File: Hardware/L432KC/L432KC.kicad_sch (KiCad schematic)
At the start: 26 parts, among them J1 Conn_01x09, J2 Conn_01x07, J3 USB_B_Micro, J4 JVCC, J5 JTAG, J6 LogicAna, U1 NUCLEO-L432KC

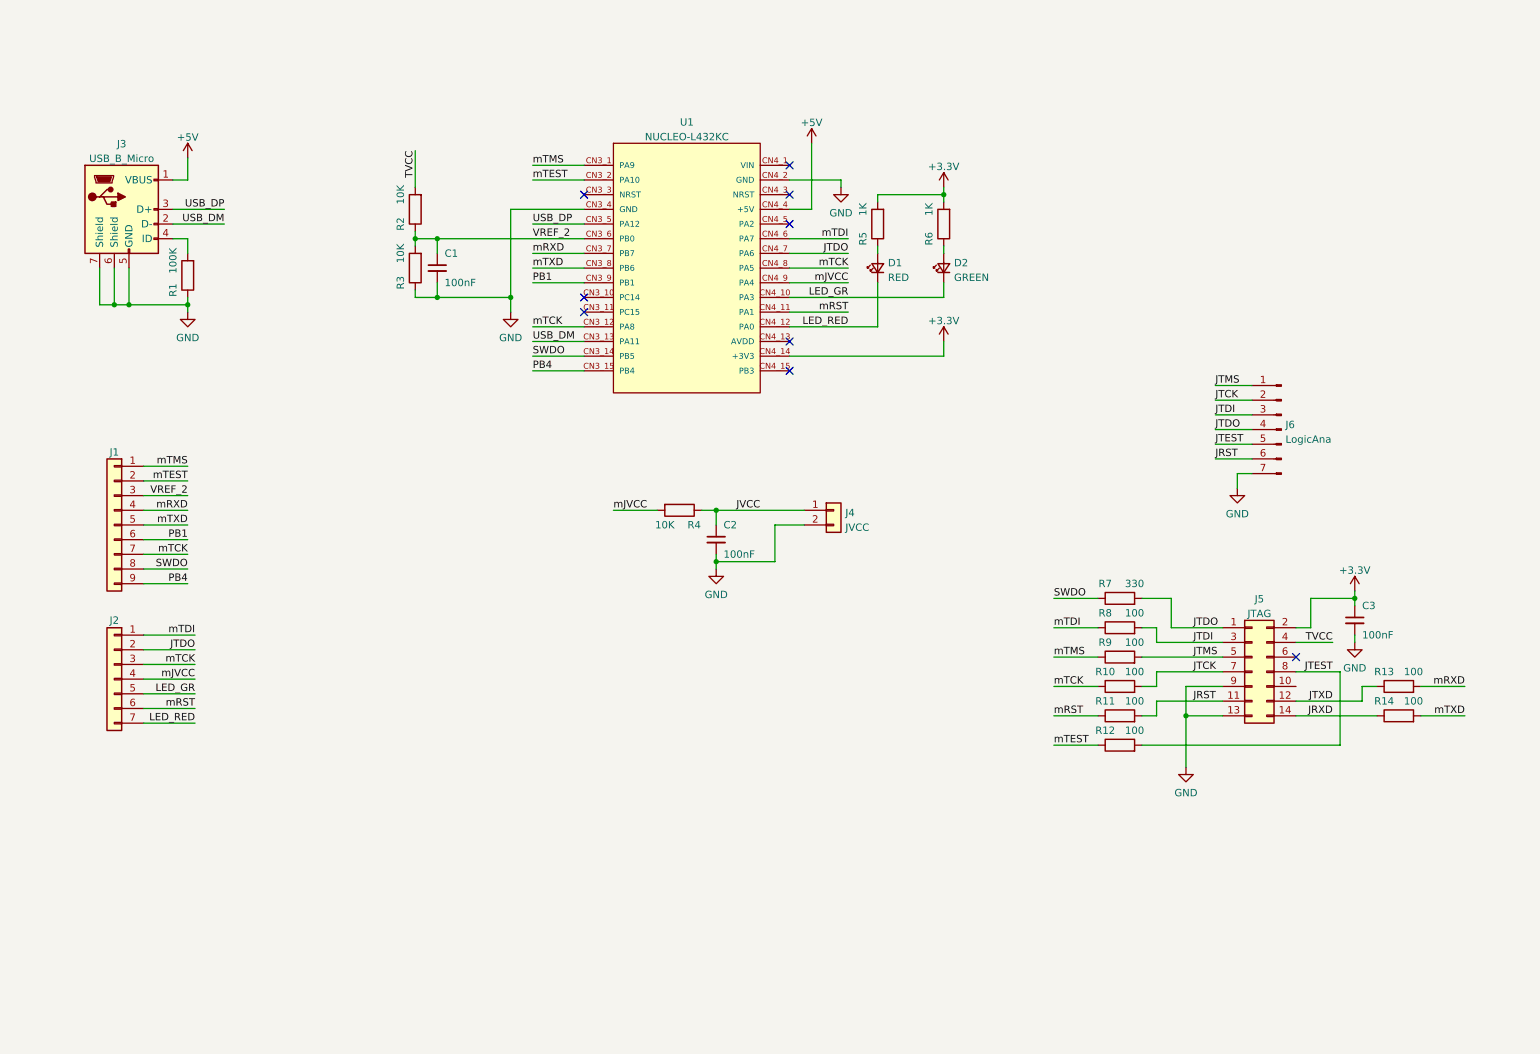
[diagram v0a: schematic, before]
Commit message: Update Hardware models - Added dual support for L432KC.
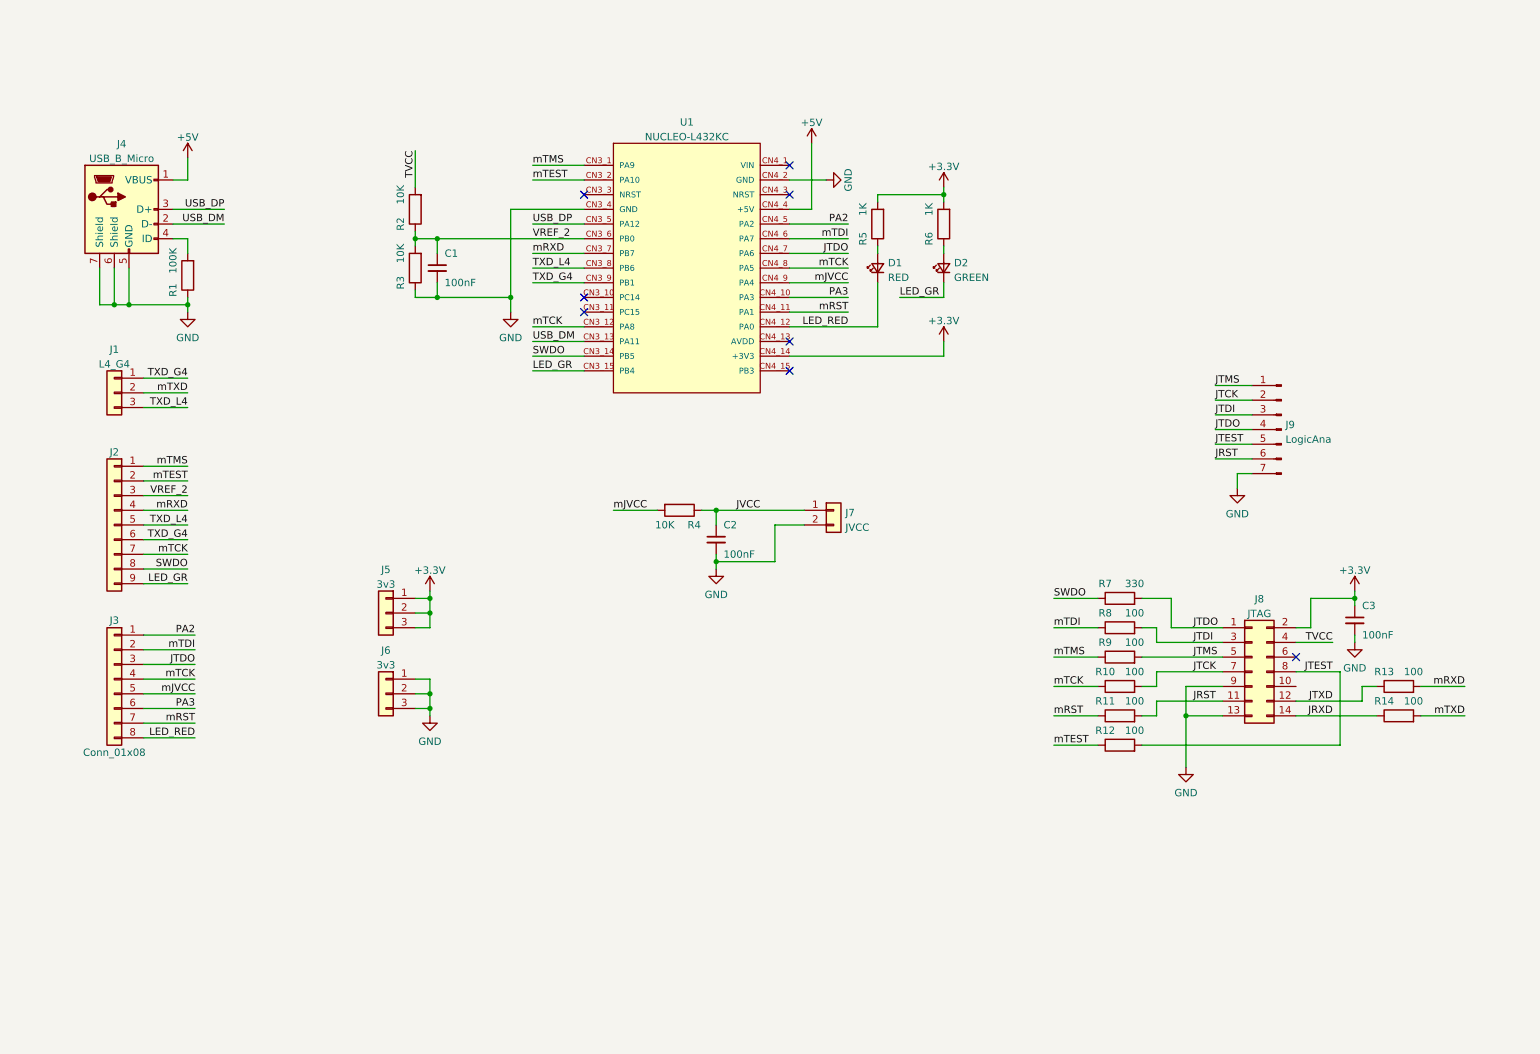
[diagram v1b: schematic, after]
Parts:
- added J1: L4_G4, Connector_PinHeader_2.54mm:PinHeader_1x03_P2.54mm_Vertical, symbol Connector_Generic:Conn_01x03
- added J5, J6: 3v3, Connector_PinHeader_2.54mm:PinHeader_1x03_P2.54mm_Vertical, symbol Connector_Generic:Conn_01x03
- J3: renamed from J2; value Conn_01x07 -> Conn_01x08; footprint Connector_PinHeader_2.54mm:PinHeader_1x07_P2.54mm_Vertical -> Connector_PinHeader_2.54mm:PinHeader_1x08_P2.54mm_Vertical; symbol Connector_Generic:Conn_01x07 -> Connector_Generic:Conn_01x08
- renumbered J1 to J2, J3 to J4, J4 to J7, J5 to J8, J6 to J9
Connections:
- net PB4 is gone; now on net LED_GR: J2.9 (Pin_9), U1.CN3_15 (PB4)
- net +3.3V: now also J5.1 (Pin_1), J5.2 (Pin_2), J5.3 (Pin_3)
- net GND: now also J6.1 (Pin_1), J6.2 (Pin_2), J6.3 (Pin_3)
- net JTDO: now also J3.3 (Pin_3); no longer J3.2 (Pin_2)
- net LED_GR: no longer J3.5 (Pin_5), U1.CN4_10 (PA3)
- net LED_RED: now also J3.8 (Pin_8); no longer J3.7 (Pin_7)
- net mJVCC: now also J3.5 (Pin_5); no longer J3.4 (Pin_4)
- net mRST: now also J3.7 (Pin_7); no longer J3.6 (Pin_6)
- net mTCK: now also J3.4 (Pin_4); no longer J3.3 (Pin_3)
- net mTDI: now also J3.2 (Pin_2); no longer J3.1 (Pin_1)
- net mTXD: now also J1.2 (Pin_2); no longer J2.5 (Pin_5), U1.CN3_8 (PB6)
- net PA2: now reaches U1.CN4_5 (PA2)
- net PA2: now also J3.1 (Pin_1)
- net PB1 renamed TXD_G4
- net TXD_G4: now also J1.1 (Pin_1)
- new net PA3: J3.6 (Pin_6), U1.CN4_10 (PA3)
- new net TXD_L4: J1.3 (Pin_3), J2.5 (Pin_5), U1.CN3_8 (PB6)
- no-connect marks 9 -> 8

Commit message: Variable voltage level for the L432KC board. Minor fixes on the Blue+Blackpill board.
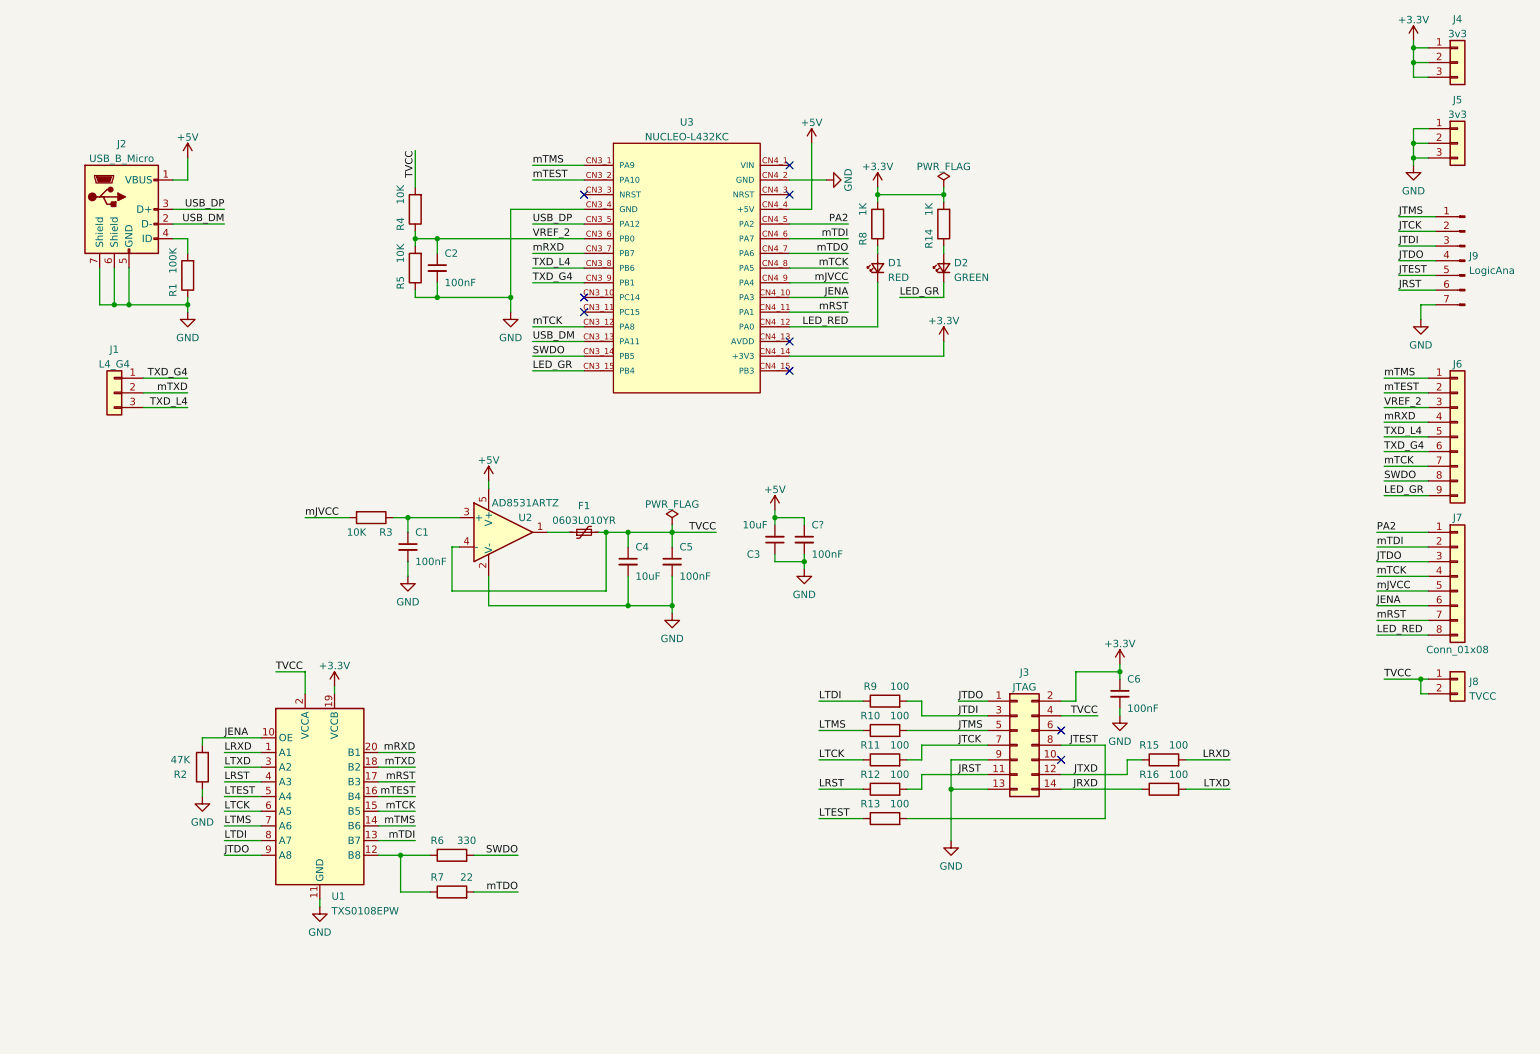
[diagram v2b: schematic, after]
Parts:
- added C3, C4: 10uF, Capacitor_SMD:C_0603_1608Metric_Pad1.08x0.95mm_HandSolder, symbol Device:C_Small
- added C5, C?: 100nF, Capacitor_SMD:C_0603_1608Metric_Pad1.08x0.95mm_HandSolder, symbol Device:C_Small
- added F1: 0603L010YR, Fuse:Fuse_0603_1608Metric_Pad1.05x0.95mm_HandSolder, symbol Device:Polyfuse_Small
- added R2: 47K, Resistor_SMD:R_0603_1608Metric_Pad0.98x0.95mm_HandSolder, symbol Device:R
- added R7: 22, Resistor_SMD:R_0603_1608Metric_Pad0.98x0.95mm_HandSolder, symbol Device:R
- added U1: TXS0108EPW, Package_SO:TSSOP-20_4.4x6.5mm_P0.65mm, symbol Logic_LevelTranslator:TXS0108EPW
- added U2: AD8531ARTZ, Package_TO_SOT_SMD:SOT-23-5_HandSoldering, symbol ad8531artz:AD8531ARTZ
- C1: renamed from C2; footprint Capacitor_THT:C_Disc_D4.3mm_W1.9mm_P5.00mm -> Capacitor_SMD:C_0603_1608Metric_Pad1.08x0.95mm_HandSolder
- C2: renamed from C1; footprint Capacitor_THT:C_Disc_D4.3mm_W1.9mm_P5.00mm -> Capacitor_SMD:C_0603_1608Metric_Pad1.08x0.95mm_HandSolder
- C6: renamed from C3; footprint Capacitor_THT:C_Disc_D4.3mm_W1.9mm_P5.00mm -> Capacitor_SMD:C_0603_1608Metric_Pad1.08x0.95mm_HandSolder
- J8: renamed from J7; value JVCC -> TVCC
- R1: footprint Resistor_THT:R_Axial_DIN0204_L3.6mm_D1.6mm_P7.62mm_Horizontal -> Resistor_SMD:R_0603_1608Metric_Pad0.98x0.95mm_HandSolder
- R10: renamed from R9; footprint Resistor_THT:R_Axial_DIN0204_L3.6mm_D1.6mm_P7.62mm_Horizontal -> Resistor_SMD:R_0603_1608Metric_Pad0.98x0.95mm_HandSolder
- R11: renamed from R10; footprint Resistor_THT:R_Axial_DIN0204_L3.6mm_D1.6mm_P7.62mm_Horizontal -> Resistor_SMD:R_0603_1608Metric_Pad0.98x0.95mm_HandSolder
- R12: renamed from R11; footprint Resistor_THT:R_Axial_DIN0204_L3.6mm_D1.6mm_P7.62mm_Horizontal -> Resistor_SMD:R_0603_1608Metric_Pad0.98x0.95mm_HandSolder
- R13: renamed from R12; footprint Resistor_THT:R_Axial_DIN0204_L3.6mm_D1.6mm_P7.62mm_Horizontal -> Resistor_SMD:R_0603_1608Metric_Pad0.98x0.95mm_HandSolder
- R14: renamed from R6; footprint Resistor_THT:R_Axial_DIN0204_L3.6mm_D1.6mm_P7.62mm_Horizontal -> Resistor_SMD:R_0603_1608Metric_Pad0.98x0.95mm_HandSolder
- R15: renamed from R13; footprint Resistor_THT:R_Axial_DIN0204_L3.6mm_D1.6mm_P7.62mm_Horizontal -> Resistor_SMD:R_0603_1608Metric_Pad0.98x0.95mm_HandSolder
- R16: renamed from R14; footprint Resistor_THT:R_Axial_DIN0204_L3.6mm_D1.6mm_P7.62mm_Horizontal -> Resistor_SMD:R_0603_1608Metric_Pad0.98x0.95mm_HandSolder
- R3: renamed from R4; footprint Resistor_THT:R_Axial_DIN0204_L3.6mm_D1.6mm_P7.62mm_Horizontal -> Resistor_SMD:R_0603_1608Metric_Pad0.98x0.95mm_HandSolder
- R4: renamed from R2; footprint Resistor_THT:R_Axial_DIN0204_L3.6mm_D1.6mm_P7.62mm_Horizontal -> Resistor_SMD:R_0603_1608Metric_Pad0.98x0.95mm_HandSolder
- R5: renamed from R3; footprint Resistor_THT:R_Axial_DIN0204_L3.6mm_D1.6mm_P7.62mm_Horizontal -> Resistor_SMD:R_0603_1608Metric_Pad0.98x0.95mm_HandSolder
- R6: renamed from R7; footprint Resistor_THT:R_Axial_DIN0204_L3.6mm_D1.6mm_P7.62mm_Horizontal -> Resistor_SMD:R_0603_1608Metric_Pad0.98x0.95mm_HandSolder
- R8: renamed from R5; footprint Resistor_THT:R_Axial_DIN0204_L3.6mm_D1.6mm_P7.62mm_Horizontal -> Resistor_SMD:R_0603_1608Metric_Pad0.98x0.95mm_HandSolder
- R9: renamed from R8; footprint Resistor_THT:R_Axial_DIN0204_L3.6mm_D1.6mm_P7.62mm_Horizontal -> Resistor_SMD:R_0603_1608Metric_Pad0.98x0.95mm_HandSolder
- renumbered J4 to J2, J8 to J3, J5 to J4, J6 to J5, J2 to J6, J3 to J7, U1 to U3
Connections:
- net +3.3V: now also U1.19 (VCCB)
- net +5V: now also C3.2, C?.1, U2.5 (V+)
- net GND: now also C3.1, C4.2, C5.2, C?.2, R2.1, U1.11 (GND), U2.2 (V-); no longer J8.2 (Pin_2)
- net JTDO: now also U1.9 (A8); no longer R6.2, U3.CN4_7 (PA6)
- net SWDO: now also R6.2; no longer R6.1
- net TVCC: now also J8.1 (Pin_1), J8.2 (Pin_2), C4.1, C5.1, F1.2, U1.2 (VCCA), U2.4 (-)
- net mRST: now also U1.17 (B3); no longer R12.1
- net mRXD: now also U1.20 (B1); no longer R15.2
- net mTCK: now also U1.15 (B5); no longer R11.1
- net mTDI: now also U1.13 (B7); no longer R9.1
- net mTEST: now also U1.16 (B4); no longer R13.1
- net mTMS: now also U1.14 (B6); no longer R10.1
- net mTXD: now also U1.18 (B2); no longer R16.2
- net JVCC: no longer names the net of C1.1, R3.1
- net JVCC: now also U2.3 (+); no longer J8.1 (Pin_1)
- net PA3 renamed JENA
- net JENA: now also R2.2, U1.10 (OE)
- new net: R6.1, R7.1, U1.12 (B8)
- new net: F1.1, U2.1
- new net LRST: R12.1, U1.4 (A3)
- new net LRXD: R15.2, U1.1 (A1)
- new net LTCK: R11.1, U1.6 (A5)
- new net LTDI: R9.1, U1.8 (A7)
- new net LTEST: R13.1, U1.5 (A4)
- new net LTMS: R10.1, U1.7 (A6)
- new net LTXD: R16.2, U1.3 (A2)
- new net mTDO: R7.2, U3.CN4_7 (PA6)
- no-connect marks 8 -> 9
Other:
- moved on the sheet: C1, C6, J3, J4, J5, J6, J7, J8, J9, R10, R11, R12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

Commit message: Improved JTAG bus impedance for BlackPill. Various enhancements for Nucleo K432KC. Added SpiBiWire Adapter.
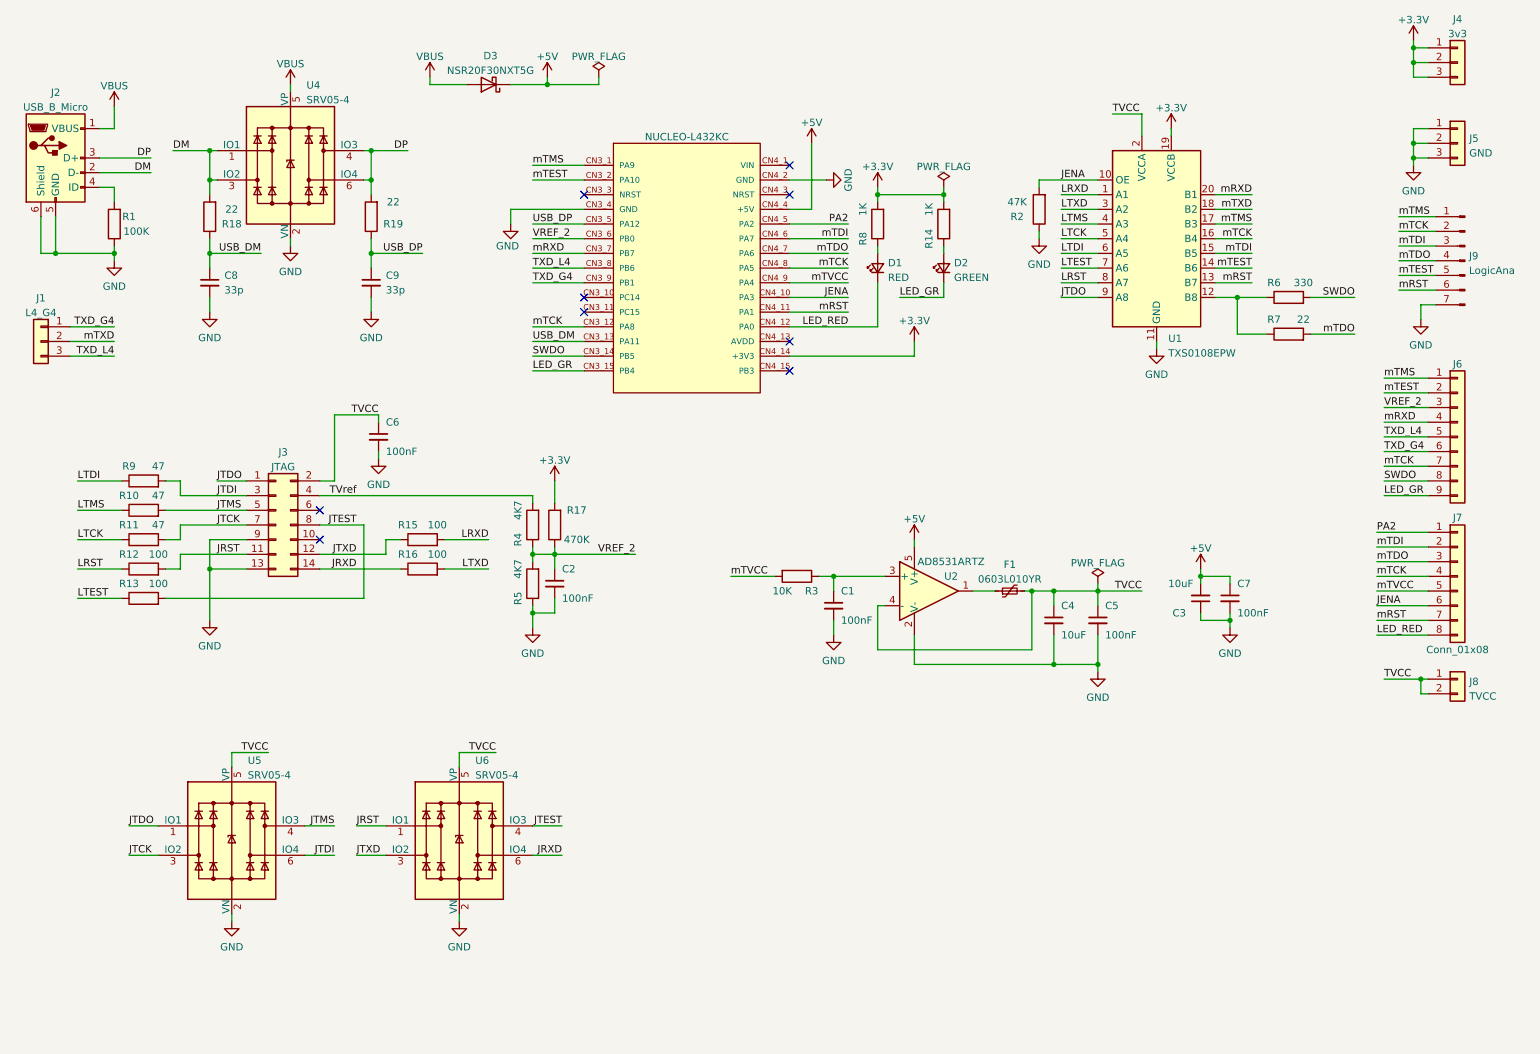
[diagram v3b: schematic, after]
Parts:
- removed J2: USB_B_Micro, lib:DEBO MICROUSB 2, symbol usb_b_micro_brkout:USB_B_Micro
- added C8, C9: 33p, Capacitor_SMD:C_0603_1608Metric_Pad1.08x0.95mm_HandSolder, symbol Device:C_Small
- added D3: NSR20F30NXT5G, Diode_SMD:D_0603_1608Metric_Pad1.05x0.95mm_HandSolder, symbol Device:D_Schottky
- added J2: USB_B_Micro, lib:USB_Micro-B_Molex-105017-0001-handsolder, symbol Connector:USB_B_Micro
- added R17: 470K, Resistor_SMD:R_0603_1608Metric_Pad0.98x0.95mm_HandSolder, symbol Device:R
- added R18, R19: 22, Resistor_SMD:R_0603_1608Metric_Pad0.98x0.95mm_HandSolder, symbol Device:R
- added U4, U5, U6: SRV05-4, Package_TO_SOT_SMD:SOT-23-6_Handsoldering, symbol Power_Protection:SRV05-4
- J5: value 3v3 -> GND
- R10, R11, R9: value 100 -> 47
- R4, R5: value 10K -> 4K7
- U3: footprint MODULE_NUCLEO-L432KC -> lib:MODULE_NUCLEO-L432KC
- gave numbers to parts that had none: 1
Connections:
- net +3.3V: now also R17.2; no longer C6.1, J3.2 (Pin_2)
- net +5V: now also D3.1 (K)
- net GND: now also C8.2, C9.2, J2.5 (GND), J2.6 (Shield), U4.2 (VN), U5.2 (VN), U6.2 (VN)
- net JRST: now also U6.1 (IO1); no longer J9.6 (Pin_6)
- net JRXD: now also U6.6 (IO4)
- net JTCK: now also U5.3 (IO2); no longer J9.2 (Pin_2)
- net JTDI: now also U5.6 (IO4); no longer J9.3 (Pin_3)
- net JTDO: now also U5.1 (IO1); no longer J7.3 (Pin_3), J9.4 (Pin_4)
- net JTEST: now also U6.4 (IO3); no longer J9.5 (Pin_5)
- net JTMS: now also U5.4 (IO3); no longer J9.1 (Pin_1)
- net JTXD: now also U6.3 (IO2)
- net LRST: now also U1.8 (A7); no longer U1.4 (A3)
- net LTCK: now also U1.5 (A4); no longer U1.6 (A5)
- net LTDI: now also U1.6 (A5); no longer U1.8 (A7)
- net LTEST: now also U1.7 (A6); no longer U1.5 (A4)
- net LTMS: now also U1.4 (A3); no longer U1.7 (A6)
- net TVCC: now also C6.1, J3.2 (Pin_2), U5.5 (VP), U6.5 (VP); no longer J3.4 (Pin_4), R4.2
- net USB_DM: now also C8.1, R18.1
- net USB_DP: now also C9.1, R19.1
- net VREF_2: now also R17.1
- net mRST: now also J9.6 (Pin_6), U1.13 (B7); no longer U1.17 (B3)
- net mTCK: now also J9.2 (Pin_2), U1.16 (B4); no longer U1.15 (B5)
- net mTDI: now also J9.3 (Pin_3), U1.15 (B5); no longer U1.13 (B7)
- net mTDO: now also J7.3 (Pin_3), J9.4 (Pin_4)
- net mTEST: now also J9.5 (Pin_5), U1.14 (B6); no longer U1.16 (B4)
- net mTMS: now also J9.1 (Pin_1), U1.17 (B3); no longer U1.14 (B6)
- net at R1.2: now also J2.4 (ID)
- net mJVCC renamed mTVCC
- new net DM: J2.2 (D-), R18.2, U4.1 (IO1), U4.3 (IO2)
- new net DP: J2.3 (D+), R19.2, U4.4 (IO3), U4.6 (IO4)
- new net TVref: J3.4 (Pin_4), R4.2
- new net VBUS: D3.2 (A), J2.1 (VBUS), U4.5 (VP)
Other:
- moved on the sheet: C1, C2, C3, C4, C5, C6, C7, F1, J1, J3, R1, R10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
